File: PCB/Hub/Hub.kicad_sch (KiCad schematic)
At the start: 31 parts, among them IC1 ESP32-DEVKITC-VE, IC2 Tranceiver_CAN, J1 Connecteur_male_Grove_Mabee, K1 Relais DSY2Y-S-205H, Q1 2N2222B, Q2 2N2222, U1 BMP581, U10 Bornier_a_vis, U3 Bornier_a_vis, U4 DB301V-5.0-2P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

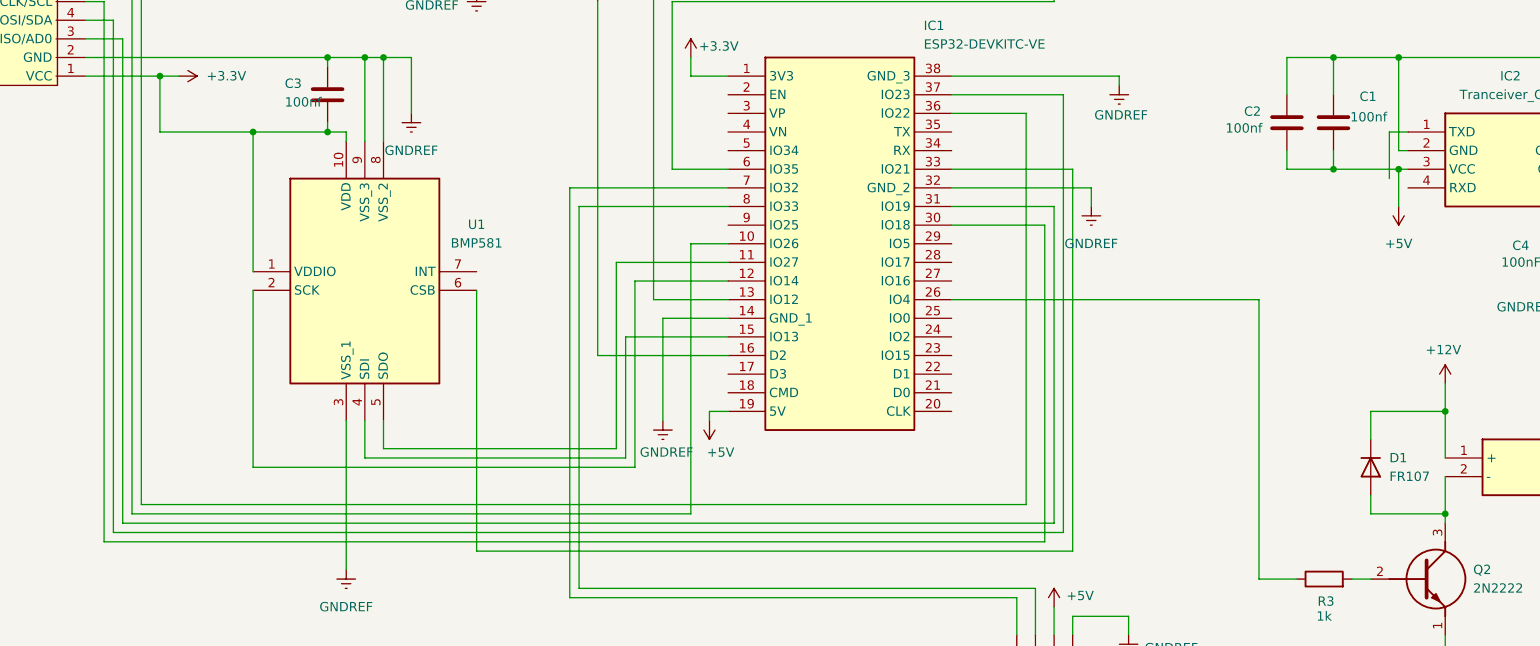
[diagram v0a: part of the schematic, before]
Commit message: MaJ Tx-Rx TCAN Hub KiCad
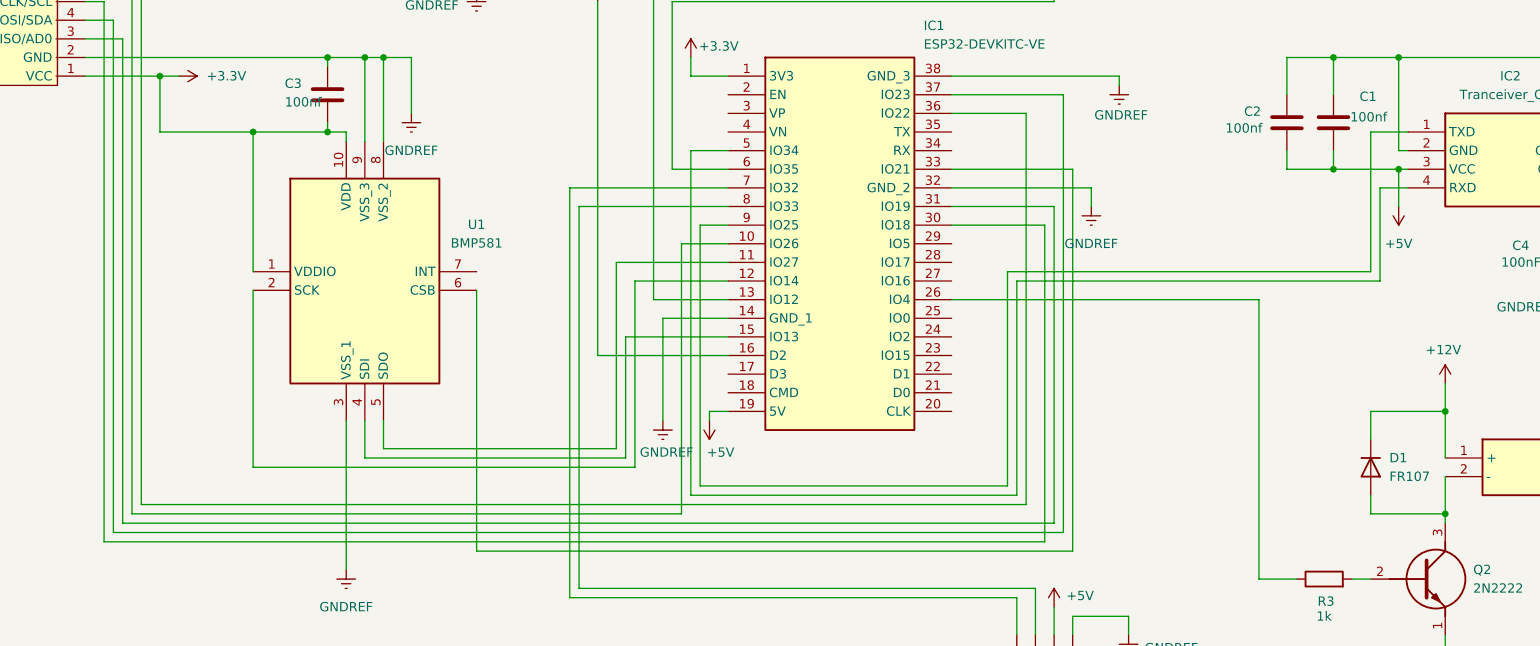
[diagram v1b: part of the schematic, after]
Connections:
- net at IC1.5 (IO34): now also IC2.4 (RXD)
- net at IC1.9 (IO25): now also IC2.1 (TXD)
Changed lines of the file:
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@@
+	(wire
+		(pts
+			(xy 125.73 91.44) (xy 125.73 127)
+		)
+		(stroke
+			(width 0)
+			(type default)
+		)
+	)
 	(wire
 		(pts
@@
 	(wire
 		(pts
+			(xy 125.73 91.44) (xy 129.54 91.44)
+		)
+		(stroke
+			(width 0)
+			(type default)
+		)
+	)
+	(wire
+		(pts
 			(xy 173.99 36.83) (xy 182.88 36.83)
 		)
@@
 	(wire
 		(pts
-			(xy 124.46 130.81) (xy 124.46 93.98)
+			(xy 123.19 130.81) (xy 123.19 93.98)
 		)
 		(stroke
@@
 	(wire
 		(pts
+			(xy 222.25 86.36) (xy 218.44 86.36)
+		)
+		(stroke
+			(width 0)
+			(type default)
+		)
+	)
+	(wire
+		(pts
 			(xy 274.32 97.79) (xy 271.78 97.79)
 		)
@@
 	(wire
 		(pts
+			(xy 168.91 128.27) (xy 124.46 128.27)
+		)
+		(stroke
+			(width 0)
+			(type default)
+		)
+	)
+	(wire
+		(pts
 			(xy 41.91 63.5) (xy 45.72 63.5)
 		)
@@
 	(wire
 		(pts
-			(xy 222.25 78.74) (xy 219.71 78.74)
+			(xy 222.25 78.74) (xy 217.17 78.74)
 		)
 		(stroke
@@
 	(wire
 		(pts
+			(xy 168.91 99.06) (xy 168.91 128.27)
+		)
+		(stroke
+			(width 0)
+			(type default)
+		)
+	)
+	(wire
+		(pts
 			(xy 124.46 68.58) (xy 124.46 71.12)
 		)
@@
 	(wire
 		(pts
+			(xy 124.46 81.28) (xy 129.54 81.28)
+		)
+		(stroke
+			(width 0)
+			(type default)
+		)
+	)
+	(wire
+		(pts
 			(xy 44.45 60.96) (xy 44.45 134.62)
 		)
@@
 	(wire
 		(pts
+			(xy 125.73 127) (xy 167.64 127)
+		)
+		(stroke
+			(width 0)
+			(type default)
+		)
+	)
+	(wire
+		(pts
 			(xy 95.25 41.91) (xy 105.41 41.91)
 		)
@@
 	(wire
 		(pts
+			(xy 124.46 128.27) (xy 124.46 81.28)
+		)
+		(stroke
+			(width 0)
+			(type default)
+		)
+	)
+	(wire
+		(pts
 			(xy 95.25 57.15) (xy 95.25 59.69)
 		)
@@
 	(wire
 		(pts
+			(xy 167.64 127) (xy 167.64 97.79)
+		)
+		(stroke
+			(width 0)
+			(type default)
+		)
+	)
+	(wire
+		(pts
 			(xy 116.84 99.06) (xy 129.54 99.06)
 		)
@@
 	(wire
 		(pts
-			(xy 124.46 93.98) (xy 129.54 93.98)
+			(xy 123.19 93.98) (xy 129.54 93.98)
 		)
 		(stroke
@@
 	(wire
 		(pts
+			(xy 218.44 99.06) (xy 168.91 99.06)
+		)
+		(stroke
+			(width 0)
+			(type default)
+		)
+	)
+	(wire
+		(pts
 			(xy 121.92 83.82) (xy 129.54 83.82)
 		)
@@
 	(wire
 		(pts
-			(xy 219.71 78.74) (xy 219.71 85.09)
-		)
-		(stroke
-			(width 0)
-			(type default)
-		)
-	)
-	(wire
-		(pts
 			(xy 121.92 60.96) (xy 121.92 83.82)
 		)
@@
 	(wire
 		(pts
-			(xy 48.26 130.81) (xy 124.46 130.81)
+			(xy 48.26 130.81) (xy 123.19 130.81)
 		)
 		(stroke
@@
 	(wire
 		(pts
+			(xy 167.64 97.79) (xy 217.17 97.79)
+		)
+		(stroke
+			(width 0)
+			(type default)
+		)
+	)
+	(wire
+		(pts
 			(xy 80.01 118.11) (xy 80.01 123.19)
 		)
@@
 	(wire
 		(pts
+			(xy 217.17 78.74) (xy 217.17 97.79)
+		)
+		(stroke
+			(width 0)
+			(type default)
+		)
+	)
+	(wire
+		(pts
 			(xy 39.37 31.75) (xy 30.48 31.75)
 		)
@@
 		)
 		(stroke
+			(width 0)
+			(type default)
+		)
+	)
+	(wire
+		(pts
+			(xy 218.44 86.36) (xy 218.44 99.06)
+		)
+		(stroke

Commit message: Validation sch HUB OUVRIER
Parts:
- removed C3: 100nf, Capacitor_THT:C_Axial_L3.8mm_D2.6mm_P7.50mm_Horizontal, symbol Device:C
- removed U1: BMP581, projet:BMP581, symbol BMP581:BMP581
- added U2: BMP581, Bibliotheque_Projet:BMP581, symbol Bibliotheque_Projet:BMP581
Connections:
- net +3.3V: now also U2.1 (VDD)
- net GNDREF: now also U2.2 (GND), U2.8 (GND)
- net at IC1.11 (IO27): now also U2.7 (SDO)
- net at IC1.12 (IO14): now also U2.3 (SCL)
- net at IC1.15 (IO13): now also U2.4 (SDI)
- net at IC1.33 (IO21): now also U2.6 (CSB)
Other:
- moved on the sheet: D1, LS1, Q2, R3

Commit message: hub
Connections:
- net +12V: now also D2.1 (K), K1.8 (NO_1), K1.9 (NO_2), U8.1 (12V); no longer K1.13 (COM_2), K1.4 (COM_1), U10.2, U3.2
- net GNDREF: now also U7.2; no longer R2.2
- net at IC1.13 (IO12): now also R2.1; no longer U7.1
- new net: R2.2, U7.1
- new net Vin: K1.13 (COM_2), K1.4 (COM_1), U10.2, U3.2
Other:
- moved on the sheet: R2
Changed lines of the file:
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@@
 	)
 	(junction
+		(at 121.92 22.86)
+		(diameter 0)
+		(color 0 0 0 0)
+	)
+	(junction
 		(at 95.25 41.91)
 		(diameter 0)
@@
 	(wire
 		(pts
+			(xy 205.74 34.29) (xy 205.74 38.1)
+		)
+		(stroke
+			(width 0)
+			(type default)
+		)
+	)
+	(wire
+		(pts
 			(xy 67.31 24.13) (xy 62.23 24.13)
 		)
@@
 	(wire
 		(pts
+			(xy 187.96 29.21) (xy 187.96 41.91)
+		)
+		(stroke
+			(width 0)
+			(type default)
+		)
+	)
+	(wire
+		(pts
 			(xy 127 31.75) (xy 154.94 31.75)
 		)
@@
 	(wire
 		(pts
-			(xy 187.96 29.21) (xy 187.96 58.42)
-		)
-		(stroke
-			(width 0)
-			(type default)
-		)
-	)
-	(wire
-		(pts
 			(xy 176.53 83.82) (xy 160.02 83.82)
 		)
@@
 	(wire
 		(pts
-			(xy 201.93 34.29) (xy 205.74 34.29)
-		)
-		(stroke
-			(width 0)
-			(type default)
-		)
-	)
-	(wire
-		(pts
 			(xy 274.32 68.58) (xy 271.78 68.58)
 		)
@@
 	(wire
 		(pts
+			(xy 190.5 34.29) (xy 205.74 34.29)
+		)
+		(stroke
+			(width 0)
+			(type default)
+		)
+	)
+	(wire
+		(pts
+			(xy 121.92 20.32) (xy 121.92 22.86)
+		)
+		(stroke
+			(width 0)
+			(type default)
+		)
+	)
+	(wire
+		(pts
 			(xy 41.91 63.5) (xy 45.72 63.5)
 		)
@@
 	(wire
 		(pts
-			(xy 205.74 34.29) (xy 205.74 38.1)
+			(xy 34.29 20.32) (xy 34.29 29.21)
 		)
 		(stroke
@@
 	(wire
 		(pts
-			(xy 34.29 20.32) (xy 34.29 29.21)
+			(xy 41.91 58.42) (xy 48.26 58.42)
 		)
 		(stroke
@@
 	(wire
 		(pts
-			(xy 41.91 58.42) (xy 48.26 58.42)
+			(xy 231.14 138.43) (xy 231.14 143.51)
 		)
 		(stroke
@@
 	(wire
 		(pts
-			(xy 231.14 138.43) (xy 231.14 143.51)
+			(xy 187.96 49.53) (xy 187.96 58.42)
 		)
 		(stroke
@@
 	(wire
 		(pts
-			(xy 190.5 34.29) (xy 194.31 34.29)
-		)
-		(stroke
-			(width 0)
-			(type default)
-		)
-	)
-	(wire
-		(pts
 			(xy 173.99 30.48) (xy 173.99 29.21)
 		)
@@
 	)
 	(symbol
+		(lib_id "power:+12V")
+		(at 121.92 20.32 0)
+		(unit 1)
+		(body_style 1)
+		(exclude_from_sim no)
+		(in_bom yes)
+		(on_board yes)
+		(in_pos_files yes)
+		(dnp no)
+		(fields_autoplaced yes)
+		(property "Reference" "#PWR07"
+			(at 121.92 24.13 0)
+			(hide yes)
+			(show_name no)
+			(do_not_autoplace no)
+			(effects
+				(font
+					(size 1.27 1.27)
+				)
+			)
+		)
+		(property "Value" "+12V"
+			(at 121.92 15.24 0)
+			(show_name no)
+			(do_not_autoplace no)
+			(effects
+				(font
+					(size 1.27 1.27)
+				)
+			)
+		)
+		(property "Footprint" ""
+			(at 121.92 20.32 0)
+			(hide yes)
+			(show_name no)
+			(do_not_autoplace no)
+			(effects
+				(font
+					(size 1.27 1.27)
+				)
+			)
+		)
+		(property "Datasheet" ""
+			(at 121.92 20.32 0)
+			(hide yes)
+			(show_name no)
+			(do_not_autoplace no)
+			(effects
+				(font
+					(size 1.27 1.27)
+				)
+			)
+		)
+		(property "Description" "Power symbol creates a global label with name \"+12V\""
+			(at 121.92 20.32 0)
+			(hide yes)
+			(show_name no)
+			(do_not_autoplace no)
+			(effects
+				(font
+					(size 1.27 1.27)
+				)
+			)
+		)
+		(pin "1"
+		)
+		(instances
+			(project "Hub"
+				(path "/08f5f273-7560-4bf5-9444-cae26833cf8d"
+					(reference "#PWR07")
+					(unit 1)
+				)
+			)
+		)
+	)
+	(symbol
 		(lib_id "Bibliotheque_Projet:Bornier_a_vis")
 		(at 24.13 21.59 180)
@@
 			)
 		)
-		(property "Value" "+12V"
+		(property "Value" "Vin"
 			(at 39.37 22.86 0)
 			(show_name no)
@@
 	(symbol
 		(lib_id "Device:R")
-		(at 198.12 34.29 90)
+		(at 187.96 45.72 180)
 		(unit 1)
 		(body_style 1)
@@
 		(dnp no)
 		(property "Reference" "R2"
-			(at 199.136 31.75 90)
+			(at 185.42 44.704 90)
 			(show_name no)
 			(do_not_autoplace no)
@@
 		)
 		(property "Value" "150"
-			(at 200.152 36.83 90)
+			(at 190.5 43.688 90)
 			(show_name no)
 			(do_not_autoplace no)
@@
 		)
 		(property "Footprint" "Resistor_THT:R_Axial_DIN0207_L6.3mm_D2.5mm_P10.16mm_Horizontal"
-			(at 198.12 36.068 90)
+			(at 189.738 45.72 90)
 			(hide yes)
 			(show_name no)
@@
 		)
 		(property "Datasheet" ""
-			(at 198.12 34.29 0)
+			(at 187.96 45.72 0)
 			(hide yes)
 			(show_name no)
@@
 		)
 		(property "Description" "Resistor"
-			(at 198.12 34.29 0)
+			(at 187.96 45.72 0)
 			(hide yes)
 			(show_name no)
@@
 			)
 		)
-		(property "Value" "+12V"
+		(property "Value" "Vin"
 			(at 107.95 17.78 0)
 			(show_name no)

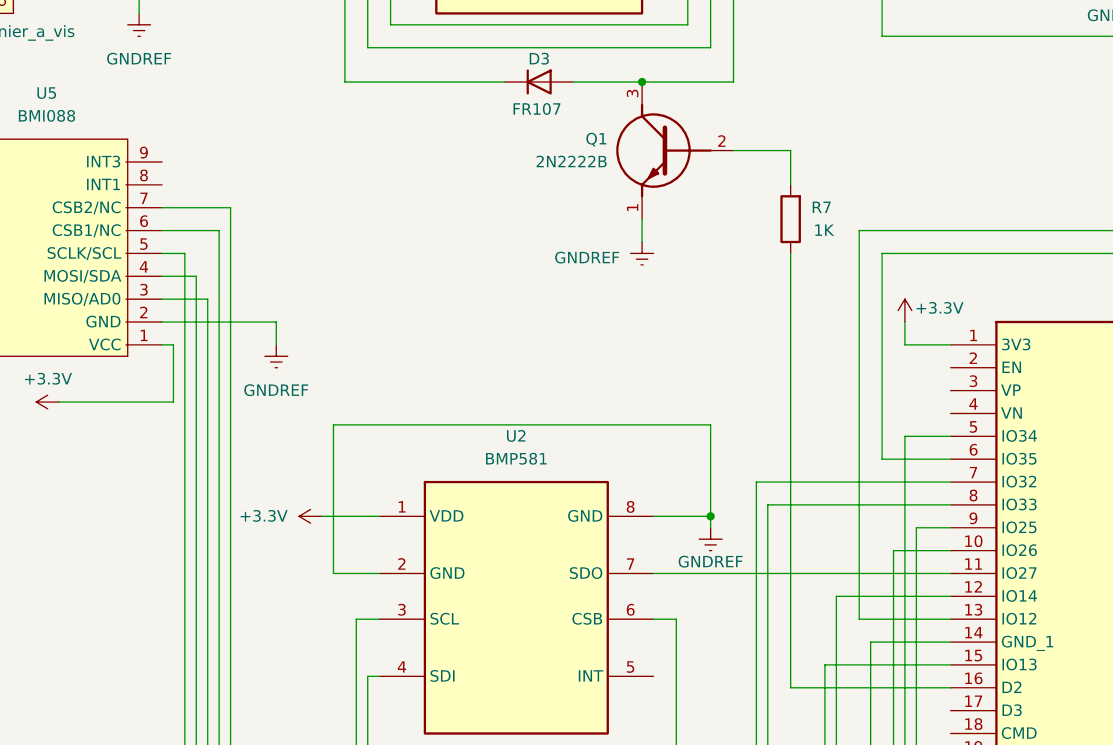
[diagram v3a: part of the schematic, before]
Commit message: connected INT pins BMI088 KiCad Hub
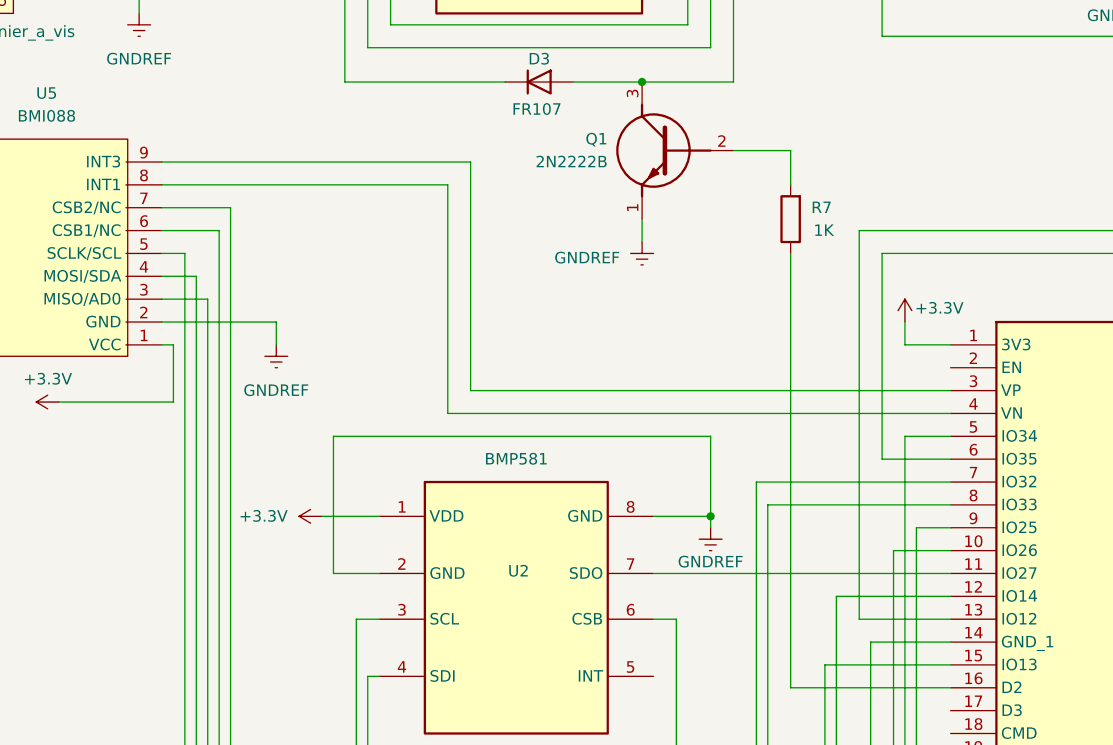
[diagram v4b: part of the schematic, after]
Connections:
- net at IC1.3 (VP): now also U5.9 (INT3)
- net at IC1.4 (VN): now also U5.8 (INT1)
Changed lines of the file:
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@@
 	)
 	(junction
-		(at 102.87 90.17)
-		(diameter 0)
-		(color 0 0 0 0)
-	)
-	(junction
 		(at 231.14 129.54)
 		(diameter 0)
@@
 	)
 	(junction
+		(at 102.87 90.17)
+		(diameter 0)
+		(color 0 0 0 0)
+	)
+	(junction
 		(at 102.87 26.67)
 		(diameter 0)
@@
 	(wire
 		(pts
+			(xy 76.2 76.2) (xy 129.54 76.2)
+		)
+		(stroke
+			(width 0)
+			(type default)
+		)
+	)
+	(wire
+		(pts
 			(xy 176.53 144.78) (xy 176.53 147.32)
 		)
@@
 	(wire
 		(pts
+			(xy 73.66 78.74) (xy 129.54 78.74)
+		)
+		(stroke
+			(width 0)
+			(type default)
+		)
+	)
+	(wire
+		(pts
 			(xy 274.32 68.58) (xy 271.78 68.58)
 		)
@@
 	(wire
 		(pts
+			(xy 41.91 50.8) (xy 76.2 50.8)
+		)
+		(stroke
+			(width 0)
+			(type default)
+		)
+	)
+	(wire
+		(pts
 			(xy 154.94 31.75) (xy 154.94 33.02)
 		)
@@
 	(wire
 		(pts
+			(xy 73.66 53.34) (xy 73.66 78.74)
+		)
+		(stroke
+			(width 0)
+			(type default)
+		)
+	)
+	(wire
+		(pts
 			(xy 46.99 132.08) (xy 173.99 132.08)
 		)
@@
 	(wire
 		(pts
+			(xy 76.2 50.8) (xy 76.2 76.2)
+		)
+		(stroke
+			(width 0)
+			(type default)
+		)
+	)
+	(wire
+		(pts
 			(xy 62.23 24.13) (xy 62.23 41.91)
 		)
@@
 	(wire
 		(pts
-			(xy 60.96 96.52) (xy 60.96 80.01)
+			(xy 60.96 96.52) (xy 60.96 81.28)
 		)
 		(stroke
@@
 	(wire
 		(pts
-			(xy 102.87 80.01) (xy 102.87 90.17)
+			(xy 102.87 81.28) (xy 102.87 90.17)
 		)
 		(stroke
@@
 	(wire
 		(pts
-			(xy 60.96 80.01) (xy 102.87 80.01)
+			(xy 60.96 81.28) (xy 102.87 81.28)
 		)
 		(stroke
@@
 	(wire
 		(pts
+			(xy 41.91 53.34) (xy 73.66 53.34)
+		)
+		(stroke
+			(width 0)
+			(type default)
+		)
+	)
+	(wire
+		(pts
 			(xy 172.72 91.44) (xy 160.02 91.44)
 		)
@@
 		(in_pos_files yes)
 		(dnp no)
-		(fields_autoplaced yes)
 		(property "Reference" "U2"
-			(at 81.28 81.28 0)
+			(at 81.534 96.266 0)
 			(show_name no)
 			(do_not_autoplace no)

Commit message: Pin INT BMPA581 connecté KiCad Hub
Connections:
- net at IC1.29 (IO5): now also U2.6 (CSB)
- net at IC1.33 (IO21): now also U2.5 (INT); no longer U2.6 (CSB)
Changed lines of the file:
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@@
+	(wire
+		(pts
+			(xy 96.52 101.6) (xy 100.33 101.6)
+		)
+		(stroke
+			(width 0)
+			(type default)
+		)
+	)
 	(wire
 		(pts
@@
 	(wire
 		(pts
-			(xy 96.52 101.6) (xy 99.06 101.6)
-		)
-		(stroke
-			(width 0)
-			(type default)
-		)
-	)
-	(wire
-		(pts
 			(xy 129.54 104.14) (xy 120.65 104.14)
 		)
@@
 	(wire
 		(pts
+			(xy 99.06 107.95) (xy 99.06 135.89)
+		)
+		(stroke
+			(width 0)
+			(type default)
+		)
+	)
+	(wire
+		(pts
 			(xy 105.41 41.91) (xy 105.41 24.13)
 		)
@@
 	(wire
 		(pts
+			(xy 96.52 107.95) (xy 99.06 107.95)
+		)
+		(stroke
+			(width 0)
+			(type default)
+		)
+	)
+	(wire
+		(pts
 			(xy 231.14 160.02) (xy 231.14 162.56)
 		)
@@
 	(wire
 		(pts
+			(xy 166.37 93.98) (xy 160.02 93.98)
+		)
+		(stroke
+			(width 0)
+			(type default)
+		)
+	)
+	(wire
+		(pts
 			(xy 105.41 24.13) (xy 100.33 24.13)
 		)
@@
 	(wire
 		(pts
-			(xy 99.06 101.6) (xy 99.06 135.89)
-		)
-		(stroke
-			(width 0)
-			(type default)
-		)
-	)
-	(wire
-		(pts
 			(xy 121.92 22.86) (xy 129.54 22.86)
 		)
@@
 	(wire
 		(pts
+			(xy 100.33 125.73) (xy 166.37 125.73)
+		)
+		(stroke
+			(width 0)
+			(type default)
+		)
+	)
+	(wire
+		(pts
 			(xy 250.19 77.47) (xy 250.19 78.74)
 		)
@@
 	(wire
 		(pts
+			(xy 100.33 101.6) (xy 100.33 125.73)
+		)
+		(stroke
+			(width 0)
+			(type default)
+		)
+	)
+	(wire
+		(pts
 			(xy 41.91 53.34) (xy 73.66 53.34)
 		)
 		(stroke
+			(width 0)
+			(type default)
+		)
+	)
+	(wire
+		(pts
+			(xy 166.37 125.73) (xy 166.37 93.98)
+		)
+		(stroke

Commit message: correction bouton PCB Kicad
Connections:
- net +12V: no longer U6.1
- net Vin: now also U6.1
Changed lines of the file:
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@@
+	)
+	(symbol
+		(lib_id "power:+12V")
+		(at 173.99 29.21 0)
+		(unit 1)
+		(body_style 1)
+		(exclude_from_sim no)
+		(in_bom yes)
+		(on_board yes)
+		(in_pos_files yes)
+		(dnp no)
+		(property "Reference" "#PWR022"
+			(at 173.99 33.02 0)
+			(hide yes)
+			(show_name no)
+			(do_not_autoplace no)
+			(effects
+				(font
+					(size 1.27 1.27)
+				)
+			)
+		)
+		(property "Value" "Vin"
+			(at 173.99 25.4 0)
+			(show_name no)
+			(do_not_autoplace no)
+			(effects
+				(font
+					(size 1.27 1.27)
+				)
+			)
+		)
+		(property "Footprint" ""
+			(at 173.99 29.21 0)
+			(hide yes)
+			(show_name no)
+			(do_not_autoplace no)
+			(effects
+				(font
+					(size 1.27 1.27)
+				)
+			)
+		)
+		(property "Datasheet" ""
+			(at 173.99 29.21 0)
+			(hide yes)
+			(show_name no)
+			(do_not_autoplace no)
+			(effects
+				(font
+					(size 1.27 1.27)
+				)
+			)
+		)
+		(property "Description" "Power symbol creates a global label with name \"+12V\""
+			(at 173.99 29.21 0)
+			(hide yes)
+			(show_name no)
+			(do_not_autoplace no)
+			(effects
+				(font
+					(size 1.27 1.27)
+				)
+			)
+		)
+		(pin "1"
+		)
+		(instances
+			(project "Hub"
+				(path "/08f5f273-7560-4bf5-9444-cae26833cf8d"
+					(reference "#PWR022")
+					(unit 1)
+				)
+			)
+		)
 	)
 	(symbol
@@
 					(unit 1)
 				)
-			)
-		)
-	)
-	(symbol
-		(lib_id "power:+12V")
-		(at 173.99 29.21 0)
-		(unit 1)
-		(body_style 1)
-		(exclude_from_sim no)
-		(in_bom yes)
-		(on_board yes)
-		(in_pos_files yes)
-		(dnp no)
-		(property "Reference" "#PWR022"
-			(at 173.99 33.02 0)
-			(hide yes)
-			(show_name no)
-			(do_not_autoplace no)
-			(effects
-				(font
-					(size 1.27 1.27)
-				)
-			)
-		)
-		(property "Value" "+12V"
-			(at 170.688 25.146 0)
-			(show_name no)
-			(do_not_autoplace no)
-			(effects
-				(font
-					(size 1.27 1.27)
-				)
-				(justify left)
-			)
-		)
-		(property "Footprint" ""
-			(at 173.99 29.21 0)
-			(hide yes)
-			(show_name no)
-			(do_not_autoplace no)
-			(effects
-				(font
-					(size 1.27 1.27)
-				)
-			)
-		)
-		(property "Datasheet" ""
-			(at 173.99 29.21 0)
-			(hide yes)
-			(show_name no)
-			(do_not_autoplace no)
-			(effects
-				(font
-					(size 1.27 1.27)
-				)
-			)
-		)
-		(property "Description" "Power symbol creates a global label with name \"+12V\""
-			(at 173.99 29.21 0)
-			(hide yes)
-			(show_name no)
-			(do_not_autoplace no)
-			(effects
-				(font
-					(size 1.27 1.27)
-				)
-			)
-		)
-		(pin "1"
-		)
-		(instances
-			(project "Hub"
-				(path "/08f5f273-7560-4bf5-9444-cae26833cf8d"
-					(reference "#PWR022")
-					(unit 1)
-				)
